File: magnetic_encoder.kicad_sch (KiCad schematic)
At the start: 10 parts, among them J1 Conn_01x03_Pin, J2 Conn_01x04_Pin, J3 Conn_01x06_Pin, J4 Conn_01x01_Pin, U1 MT6835GT_STD

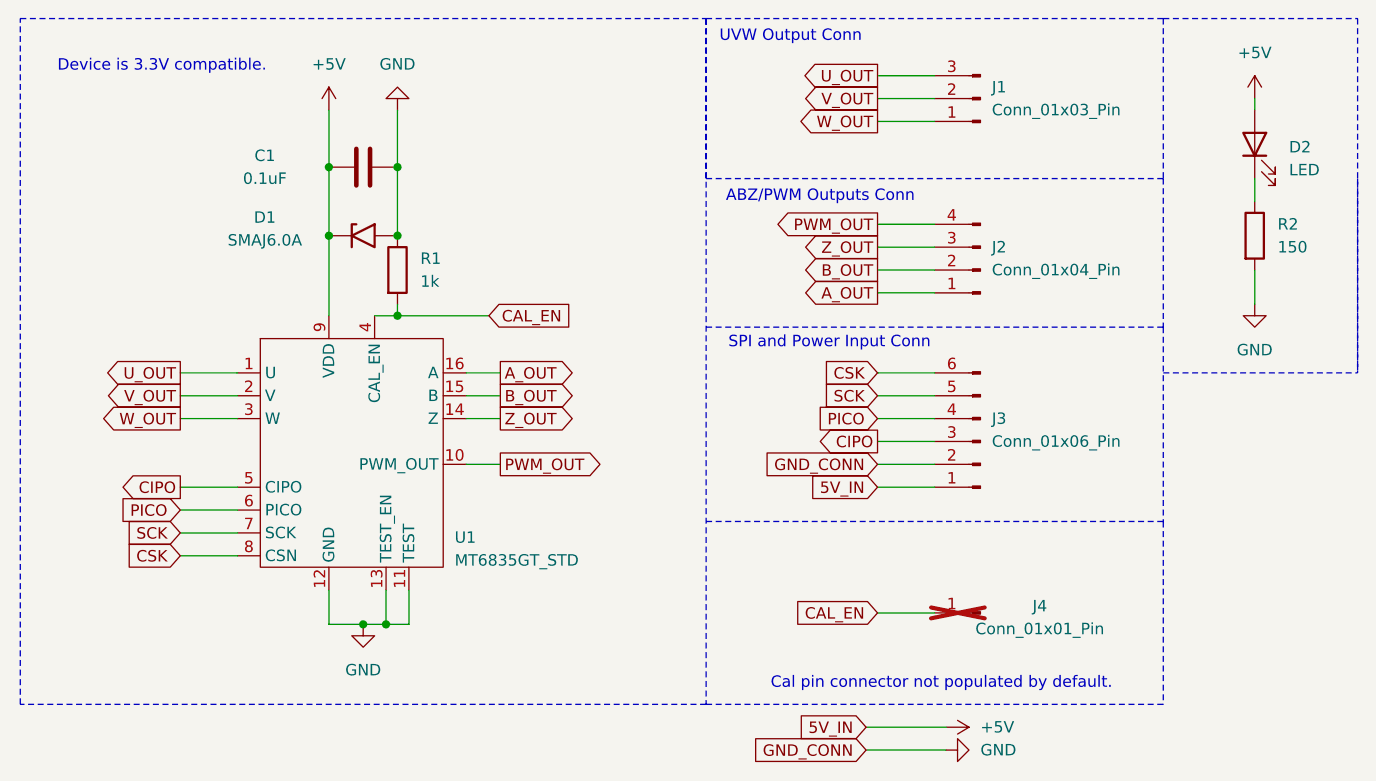
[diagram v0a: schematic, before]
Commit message: added labels to pins
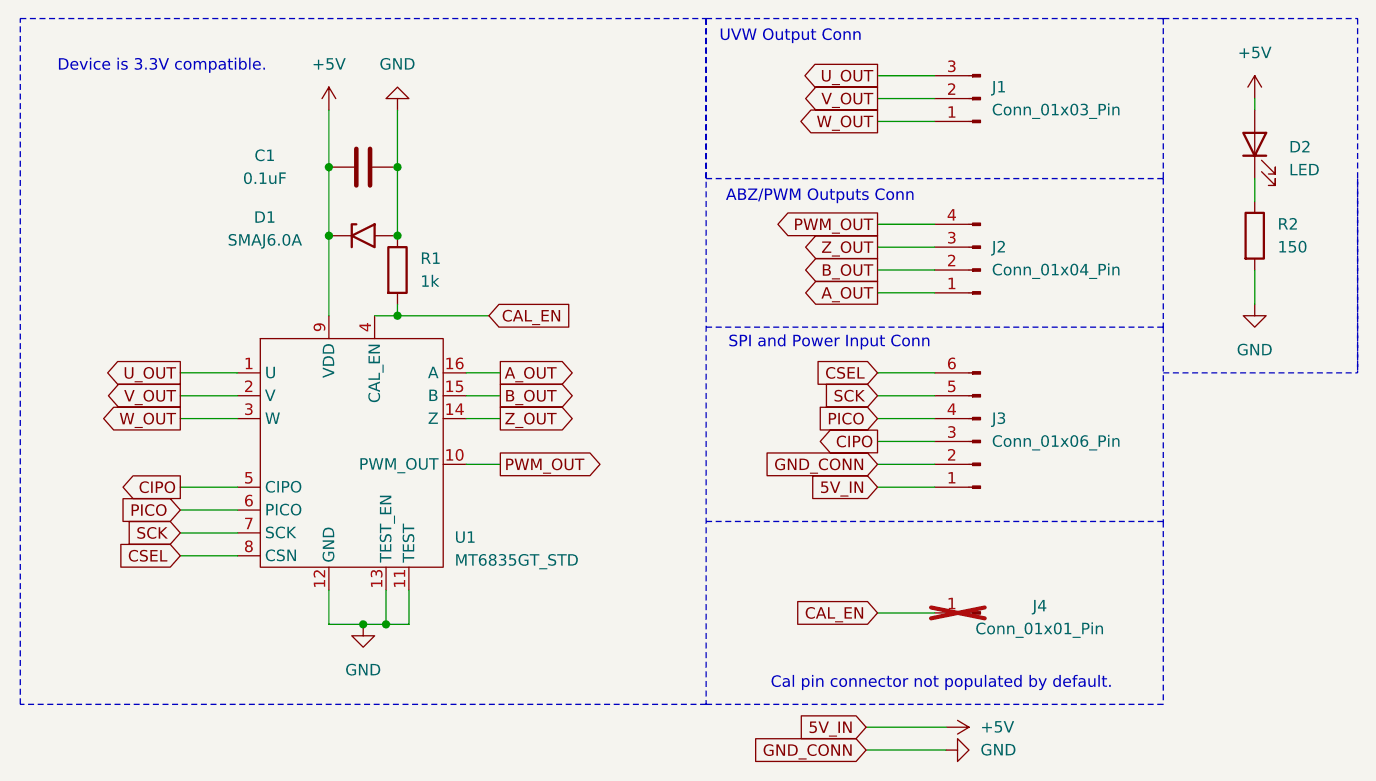
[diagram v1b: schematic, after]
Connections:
- net CSK  renamed CSEL
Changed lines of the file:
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@@
 		)
 	)
-	(global_label "CSK "
+	(global_label "CSEL"
 		(shape input)
 		(at 30.48 72.39 180)
@@
 		)
 		(property "Intersheetrefs" "${INTERSHEET_REFS}"
-			(at 22.7777 72.39 0)
+			(at 22.8382 72.39 0)
 			(effects
 				(font
@@
 		)
 	)
-	(global_label "CSK "
+	(global_label "CSEL"
 		(shape input)
 		(at 107.95 52.07 180)
@@
 		)
 		(property "Intersheetrefs" "${INTERSHEET_REFS}"
-			(at 100.2477 52.07 0)
+			(at 100.3082 52.07 0)
 			(effects
 				(font
